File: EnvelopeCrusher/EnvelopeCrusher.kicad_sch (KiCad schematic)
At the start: 4 parts, among them J4 Conn_01x02, SW1 SW_SPDT

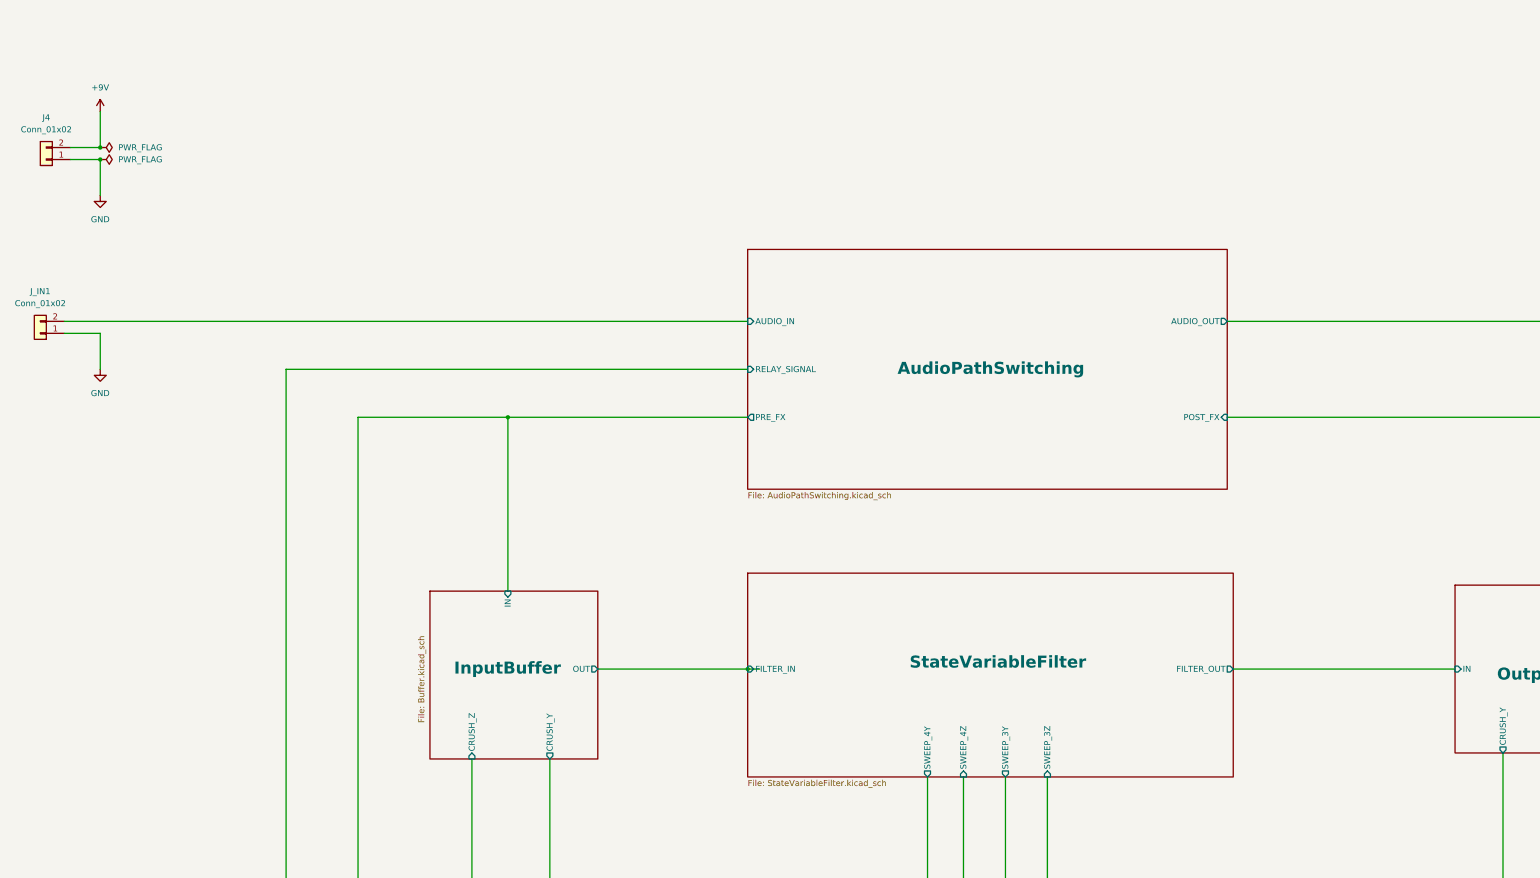
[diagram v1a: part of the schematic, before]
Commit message: updated schematic
- Added values and comments to state-variable filter block
- Updated footprints
- Changed Dual Op Amp: TL072 to AM358
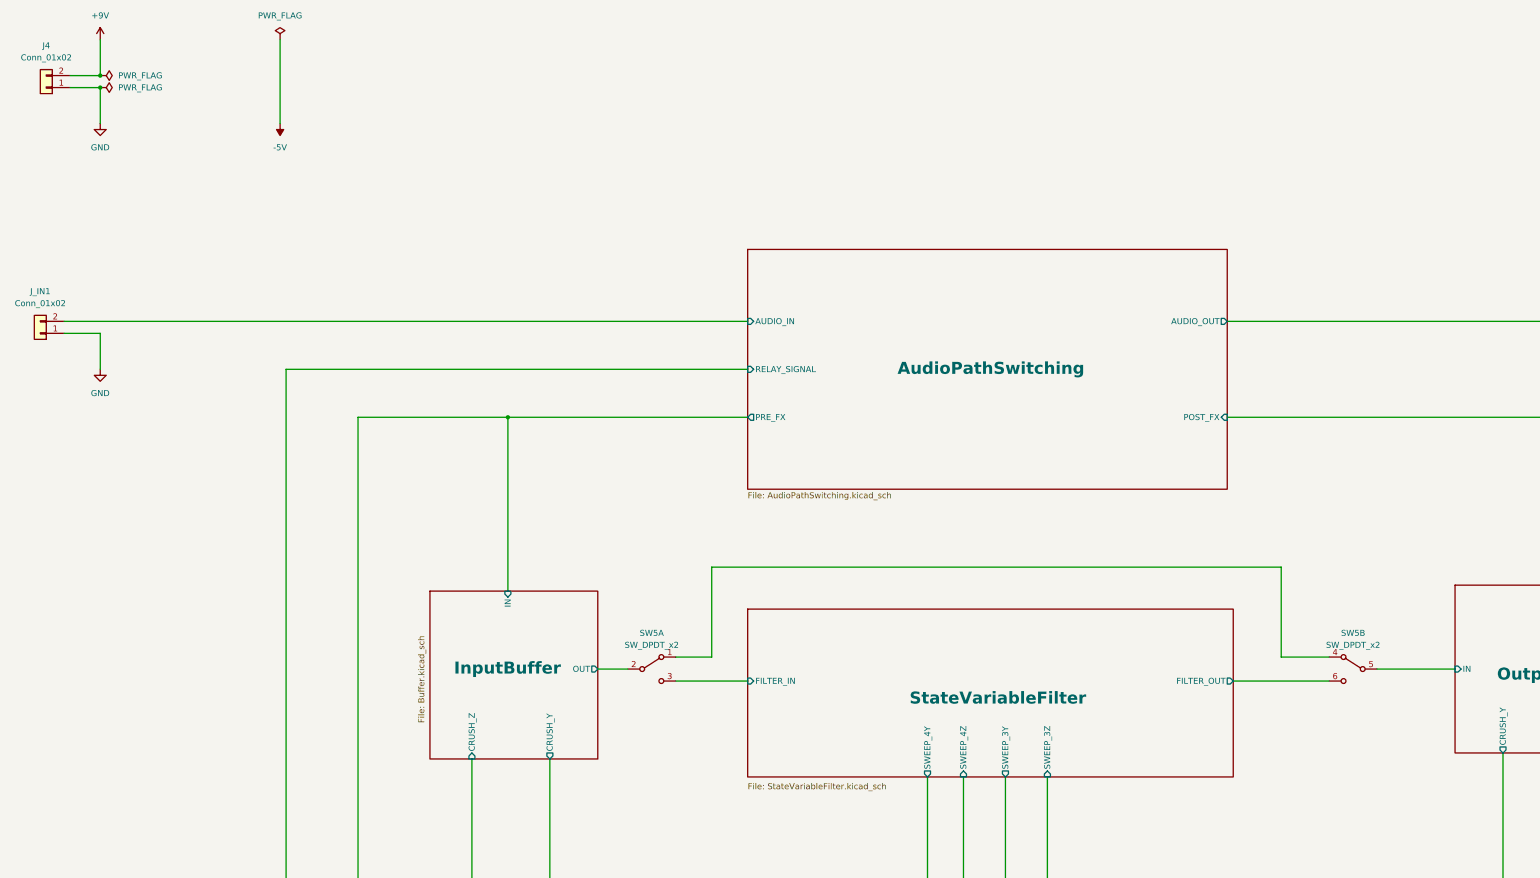
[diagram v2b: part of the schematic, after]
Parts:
- added SW5: SW_DPDT_x2, symbol Switch:SW_DPDT_x2
- J4: footprint (none) -> Connector_PinHeader_2.54mm:PinHeader_1x02_P2.54mm_Vertical
- SW1: footprint (none) -> Resistor_SMD:R_0805_2012Metric_Pad1.20x1.40mm_HandSolder
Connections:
- net InputBuffer/OUT: now also SW5.2 (B)
- net OutputBuffer/IN: now also SW5.5 (B)
- new net: SW5.1 (A), SW5.4 (A)
- new net StateVariableFilter/FILTER_IN: SW5.3 (C)
- new net StateVariableFilter/FILTER_OUT: SW5.6 (C)
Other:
- moved on the sheet: J4

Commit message: started layout
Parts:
- SW5: footprint (none) -> DailywellSwitches:Dailywell_DPDT
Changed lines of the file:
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@@
     (property "Reference" "SW5" (id 0) (at 233.68 177.8 0))
     (property "Value" "SW_DPDT_x2" (id 1) (at 233.68 180.34 0))
-    (property "Footprint" "" (id 2) (at 233.68 185.42 0)
+    (property "Footprint" "DailywellSwitches:Dailywell_DPDT" (id 2) (at 233.68 185.42 0)
       (effects (font (size 1.27 1.27)) hide)
     )
@@
     (property "Reference" "SW5" (id 0) (at 382.27 177.8 0))
     (property "Value" "SW_DPDT_x2" (id 1) (at 382.27 180.34 0))
-    (property "Footprint" "" (id 2) (at 382.27 185.42 0)
+    (property "Footprint" "DailywellSwitches:Dailywell_DPDT" (id 2) (at 382.27 185.42 0)
       (effects (font (size 1.27 1.27)) hide)
     )
@@
     )
     (path "/e3ac1148-cabe-4421-9798-ce3b96d0a6bd/dbbf7dec-944e-491e-81f3-629785497d6d"
-      (reference "J3") (unit 1) (value "Conn_01x04") (footprint "Connector_PinHeader_2.54mm:PinHeader_1x04_P2.54mm_Vertical")
+      (reference "J3") (unit 1) (value "Conn_01x04") (footprint "0.96inch_OLED_SSD1306:0.96inch_OLED_SSD1306")
     )
     (path "/cd1dfd36-0f58-432f-b48a-a1633e8b615a"
@@
       (reference "JP11") (unit 1) (value "SolderJumper_2_Bridged") (footprint "Jumper:SolderJumper-2_P1.3mm_Bridged_Pad1.0x1.5mm")
     )
+    (path "/e3ac1148-cabe-4421-9798-ce3b96d0a6bd/c18240b9-6b33-440c-8d5c-1744de96fa45"
+      (reference "JP12") (unit 1) (value "SolderJumper_2_Open") (footprint "Jumper:SolderJumper-2_P1.3mm_Open_Pad1.0x1.5mm")
+    )
     (path "/d37a9dd9-2de5-4fd7-a169-11276f1f8175"
       (reference "J_IN1") (unit 1) (value "Conn_01x02") (footprint "Connector_PinHeader_2.54mm:PinHeader_1x02_P2.54mm_Vertical")
@@
       (reference "SW2") (unit 1) (value "RotaryEncoder_Switch") (footprint "Rotary_Encoder:RotaryEncoder_Alps_EC11E-Switch_Vertical_H20mm")
     )
-    (path "/e3ac1148-cabe-4421-9798-ce3b96d0a6bd/4d6beb78-9723-4955-bd75-2fe3ee7504d0"
-      (reference "SW3") (unit 1) (value "SW_SPST") (footprint "")
-    )
     (path "/e3ac1148-cabe-4421-9798-ce3b96d0a6bd/b36f5182-dcf9-4a27-94da-19d85c464c4c/73cb570d-068a-47fb-9349-66347d7b9038"
-      (reference "SW4") (unit 1) (value "SW_DIP_x04") (footprint "")
+      (reference "SW4") (unit 1) (value "SW_DIP_x04") (footprint "Button_Switch_THT:SW_DIP_SPSTx04_Slide_6.7x11.72mm_W7.62mm_P2.54mm_LowProfile")
     )
     (path "/2965aae7-6f95-493e-bcb4-9770441cc211"
-      (reference "SW5") (unit 1) (value "SW_DPDT_x2") (footprint "")
+      (reference "SW5") (unit 1) (value "SW_DPDT_x2") (footprint "DailywellSwitches:Dailywell_DPDT")
     )
     (path "/cf223d76-8d83-4b19-91ea-62bbdb32f1a8"
-      (reference "SW5") (unit 2) (value "SW_DPDT_x2") (footprint "")
+      (reference "SW5") (unit 2) (value "SW_DPDT_x2") (footprint "DailywellSwitches:Dailywell_DPDT")
     )
     (path "/e3ac1148-cabe-4421-9798-ce3b96d0a6bd/b5d5b644-9a41-4782-b64d-ef9ba7d602f9"

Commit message: Updated footprints/symbol mappings
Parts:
- SW1: footprint Resistor_SMD:R_0805_2012Metric_Pad1.20x1.40mm_HandSolder -> DailywellSwitches:Dailywell_SPDT
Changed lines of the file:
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@@
       (effects (font (size 1.27 1.27)) hide)
     )
-    (property "Datasheet" "~" (id 3) (at 233.68 185.42 0)
+    (property "Datasheet" "https://www.mouser.co.uk/datasheet/2/979/Dailywell_01132020_2M_Series-1708785.pdf" (id 3) (at 233.68 185.42 0)
       (effects (font (size 1.27 1.27)) hide)
     )
@@
       (effects (font (size 1.27 1.27)) hide)
     )
-    (property "Footprint" "Resistor_SMD:R_0805_2012Metric_Pad1.20x1.40mm_HandSolder" (id 2) (at 281.94 314.96 0)
-      (effects (font (size 1.27 1.27)) hide)
-    )
-    (property "Datasheet" "~" (id 3) (at 281.94 314.96 0)
+    (property "Footprint" "DailywellSwitches:Dailywell_SPDT" (id 2) (at 281.94 314.96 0)
+      (effects (font (size 1.27 1.27)) hide)
+    )
+    (property "Datasheet" "https://www.mouser.co.uk/datasheet/2/979/Dailywell_01132020_2M_Series-1708785.pdf" (id 3) (at 281.94 314.96 0)
       (effects (font (size 1.27 1.27)) hide)
     )
@@
       (effects (font (size 1.27 1.27)) hide)
     )
-    (property "Datasheet" "~" (id 3) (at 382.27 185.42 0)
+    (property "Datasheet" "https://www.mouser.co.uk/datasheet/2/979/Dailywell_01132020_2M_Series-1708785.pdf" (id 3) (at 382.27 185.42 0)
       (effects (font (size 1.27 1.27)) hide)
     )
@@
     )
     (path "/5d00ccff-a592-4e31-88d0-efea6e6f99f5"
-      (reference "SW1") (unit 1) (value "SW_SPDT") (footprint "Resistor_SMD:R_0805_2012Metric_Pad1.20x1.40mm_HandSolder")
+      (reference "SW1") (unit 1) (value "SW_SPDT") (footprint "DailywellSwitches:Dailywell_SPDT")
     )
     (path "/e3ac1148-cabe-4421-9798-ce3b96d0a6bd/4c978eba-9c60-4dc1-859b-e699a70a5963"
@@
     )
     (path "/e3ac1148-cabe-4421-9798-ce3b96d0a6bd/ff428d36-5846-4c59-8126-a0f2bc41c5c7"
-      (reference "U16") (unit 1) (value "SE82XX-33") (footprint "Package_TO_SOT_SMD:SOT-223-3_TabPin2")
+      (reference "U16") (unit 1) (value "SE82XX-33") (footprint "Package_TO_SOT_SMD:SOT-23")
     )
     (path "/07d59659-d607-4ac1-8af8-79aab0df53d7/e5ffc028-ee77-401f-ba62-c5f6d09e2723/97dc05cc-aa31-4c52-9063-67b07afd5d4e"
-      (reference "U17") (unit 1) (value "SE82XX-50") (footprint "Package_TO_SOT_SMD:SOT-223-3_TabPin2")
+      (reference "U17") (unit 1) (value "SE82XX-50") (footprint "Package_TO_SOT_SMD:SOT-23")
     )
     (path "/07d59659-d607-4ac1-8af8-79aab0df53d7/10669849-6176-456c-afba-919eb2fa3577/97dc05cc-aa31-4c52-9063-67b07afd5d4e"
-      (reference "U18") (unit 1) (value "SE82XX-50") (footprint "Package_TO_SOT_SMD:SOT-223-3_TabPin2")
+      (reference "U18") (unit 1) (value "SE82XX-50") (footprint "Package_TO_SOT_SMD:SOT-23")
     )
     (path "/ebc6b7ad-0288-4bcb-90f7-c5fec31d608a/a8b5b07b-f4c7-4ca0-95dd-d580f553334d/97dc05cc-aa31-4c52-9063-67b07afd5d4e"
-      (reference "U19") (unit 1) (value "SE82XX-50") (footprint "Package_TO_SOT_SMD:SOT-223-3_TabPin2")
+      (reference "U19") (unit 1) (value "SE82XX-50") (footprint "Package_TO_SOT_SMD:SOT-23")
     )
     (path "/985225ff-bdf2-4faf-bf07-f44d56f5be76/a8b5b07b-f4c7-4ca0-95dd-d580f553334d/97dc05cc-aa31-4c52-9063-67b07afd5d4e"
-      (reference "U20") (unit 1) (value "SE82XX-50") (footprint "Package_TO_SOT_SMD:SOT-223-3_TabPin2")
+      (reference "U20") (unit 1) (value "SE82XX-50") (footprint "Package_TO_SOT_SMD:SOT-23")
     )
     (path "/4be05bf3-9d19-418a-9bbb-0b1edff8d325/a27db0c1-f1d2-4d0e-acdf-53a5c8049234/97dc05cc-aa31-4c52-9063-67b07afd5d4e"
-      (reference "U21") (unit 1) (value "SE82XX-50") (footprint "Package_TO_SOT_SMD:SOT-223-3_TabPin2")
+      (reference "U21") (unit 1) (value "SE82XX-50") (footprint "Package_TO_SOT_SMD:SOT-23")
     )
     (path "/e3ac1148-cabe-4421-9798-ce3b96d0a6bd/b36f5182-dcf9-4a27-94da-19d85c464c4c/2c84b367-cfcc-4fa2-81ef-877ef42bfb7c/97dc05cc-aa31-4c52-9063-67b07afd5d4e"
-      (reference "U22") (unit 1) (value "SE82XX-50") (footprint "Package_TO_SOT_SMD:SOT-223-3_TabPin2")
-    )
-  )
+      (reference "U22") (unit 1) (value "SE82XX-50") (footprint "Package_TO_SOT_SMD:SOT-23")
+    )
+  )

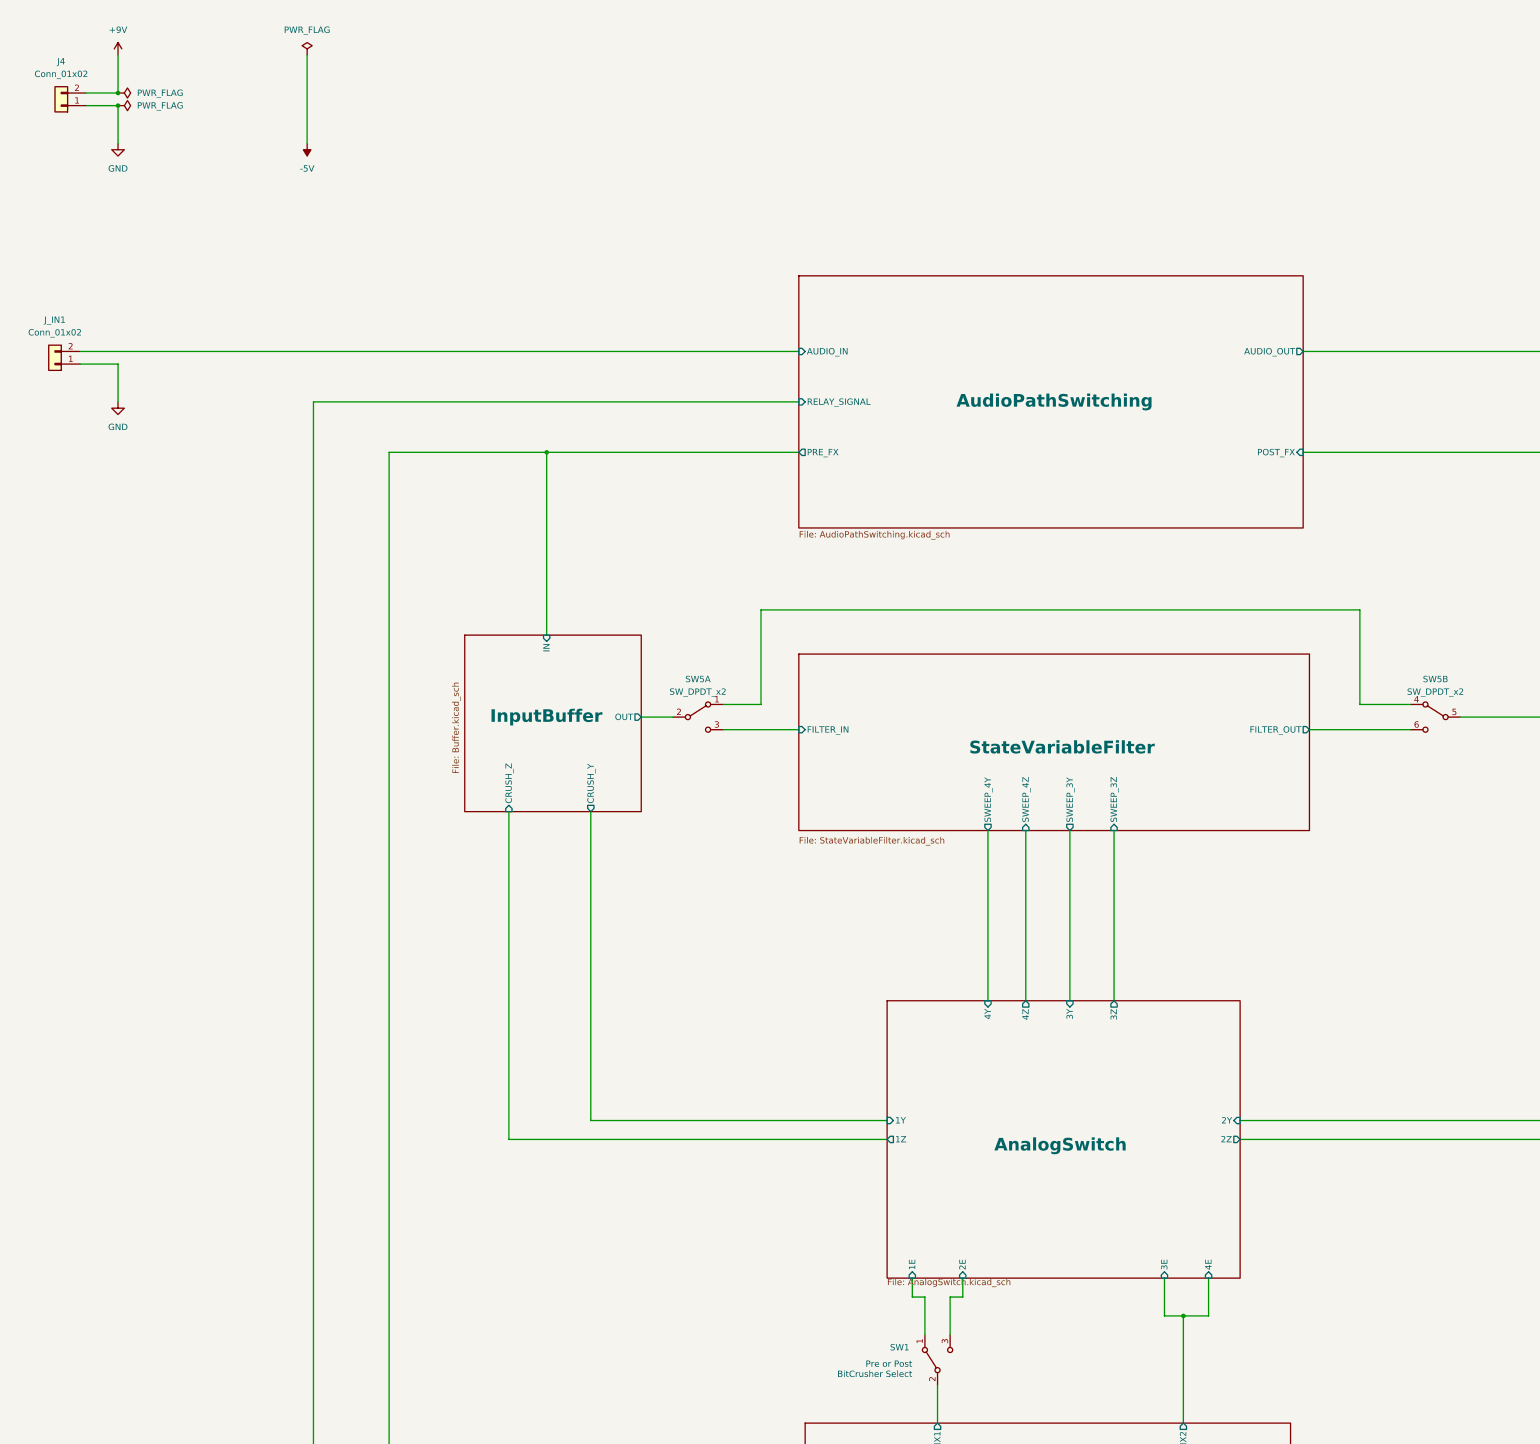
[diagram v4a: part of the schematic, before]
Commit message: organised layout into functional blocks
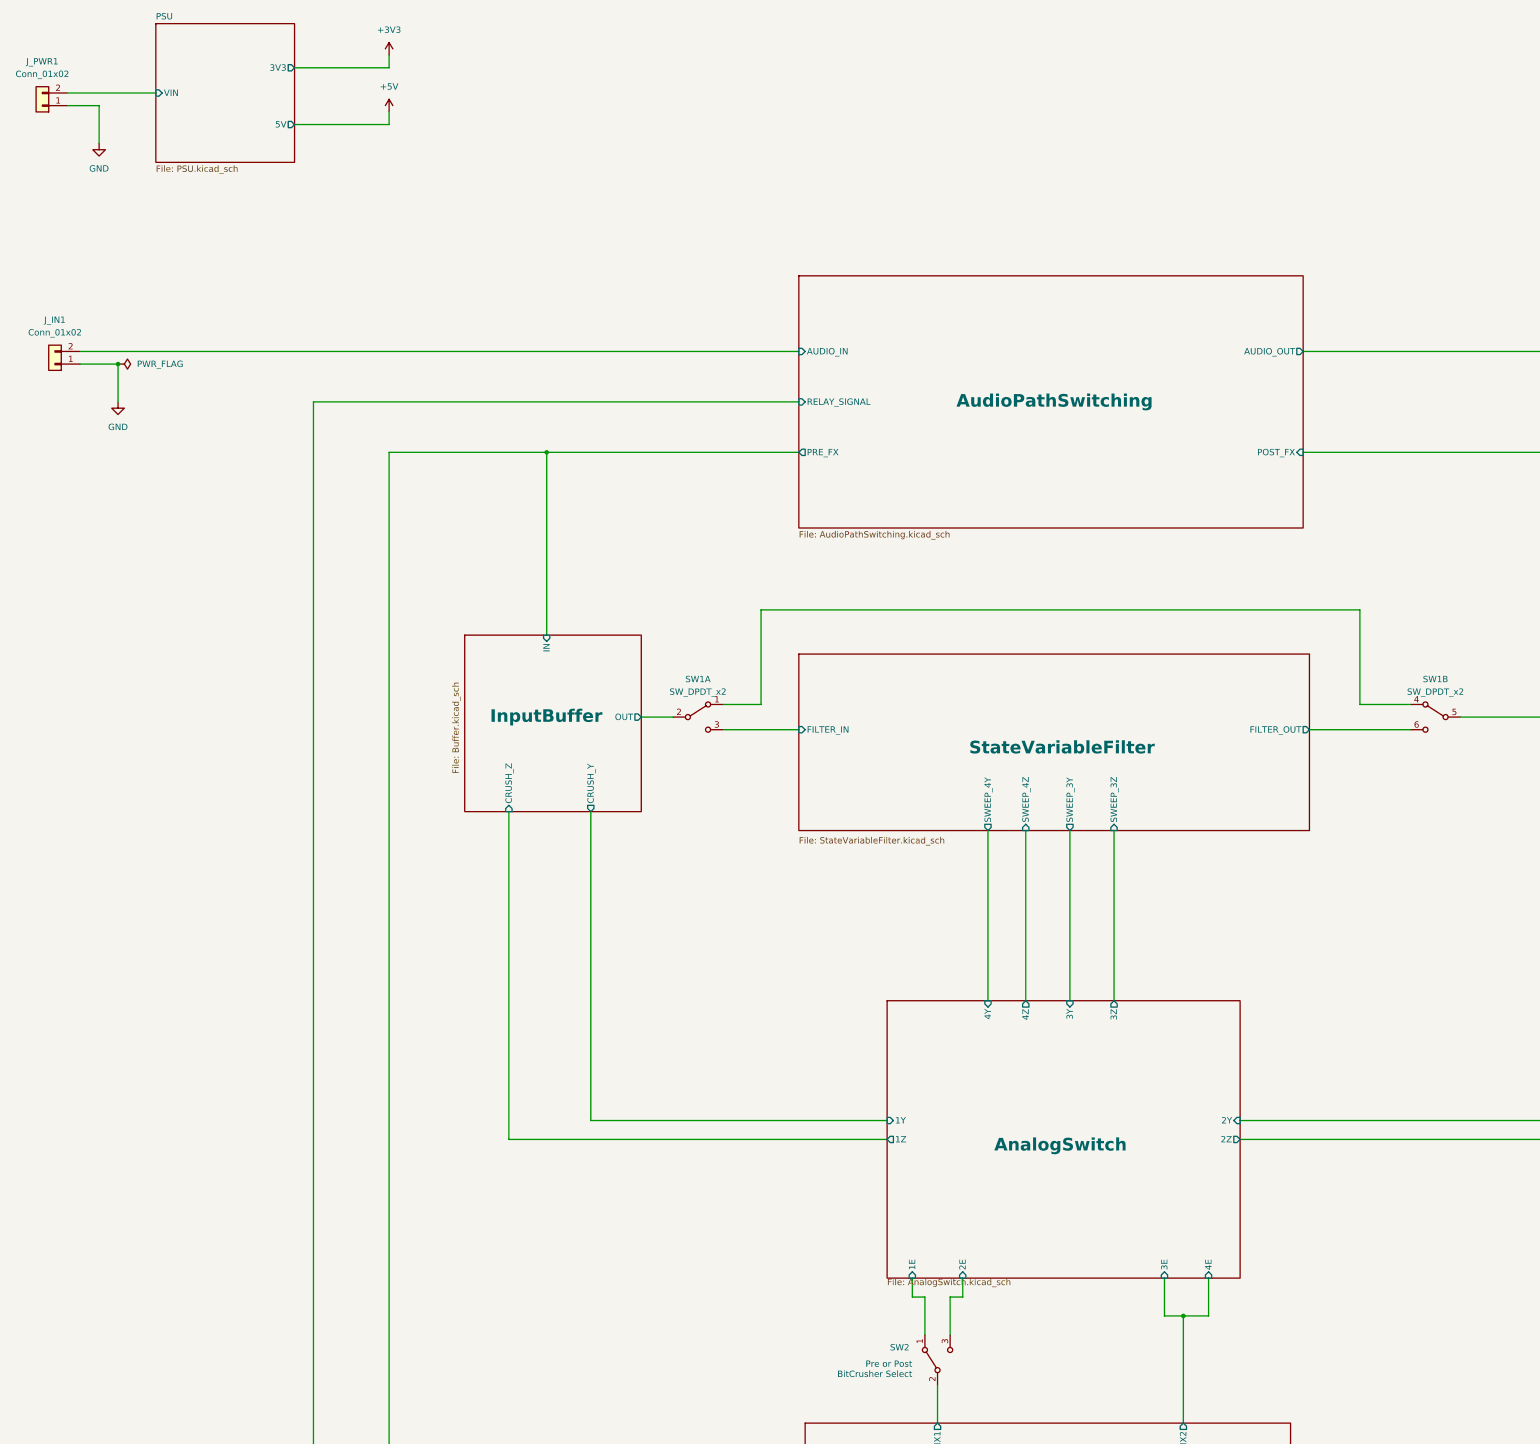
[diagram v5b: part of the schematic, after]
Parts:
- renumbered J4 to J_PWR1, SW5 to SW1, SW1 to SW2
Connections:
- net +9V renamed PSU/VIN
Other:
- added sheet PSU (PSU.kicad_sch)
- moved on the sheet: J_PWR1
